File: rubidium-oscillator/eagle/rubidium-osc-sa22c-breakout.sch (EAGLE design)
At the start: 13 parts, among them J1 OSC_TMMH-109-01-G-DV-ES-A, Q1 FDN360P, Q2 FDN360P, X1 MKDSN4, X2 MPT3, X3 MPT6, X4 SMA-142-0701-801/806, X5 SMA-142-0701-801/806, X6 SMA-142-0701-801/806

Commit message: Update rubidium-osc-sa22c-breakout.sch
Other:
- note added: "NOTE: Service and Lock are active low."
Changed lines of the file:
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@@
 <text x="157.48" y="66.04" size="1.778" layer="97">LED_GREEN</text>
 <text x="157.48" y="76.2" size="1.778" layer="97">LED_RED</text>
+<text x="91.44" y="48.26" size="1.778" layer="97">NOTE: Service and Lock are active low.</text>
 </plain>
 <instances>

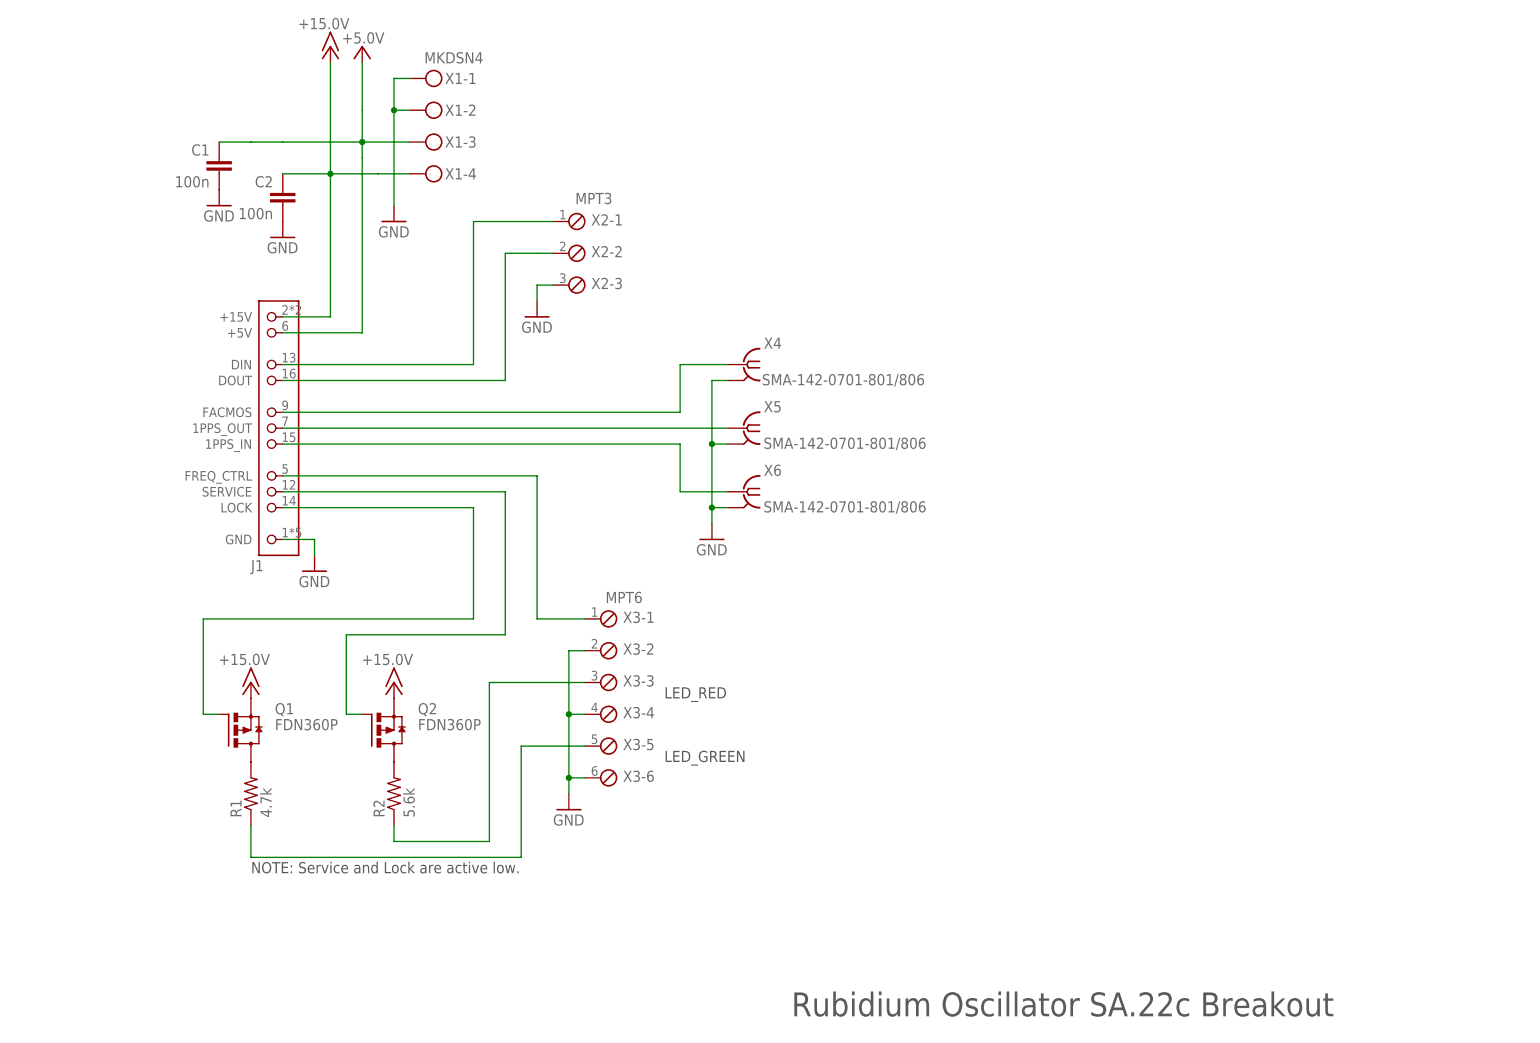
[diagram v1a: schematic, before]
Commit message: Updated rubidium osc.  Removed thermal reliefs for SMA and power grounds.  Updated p-MOSFET design.
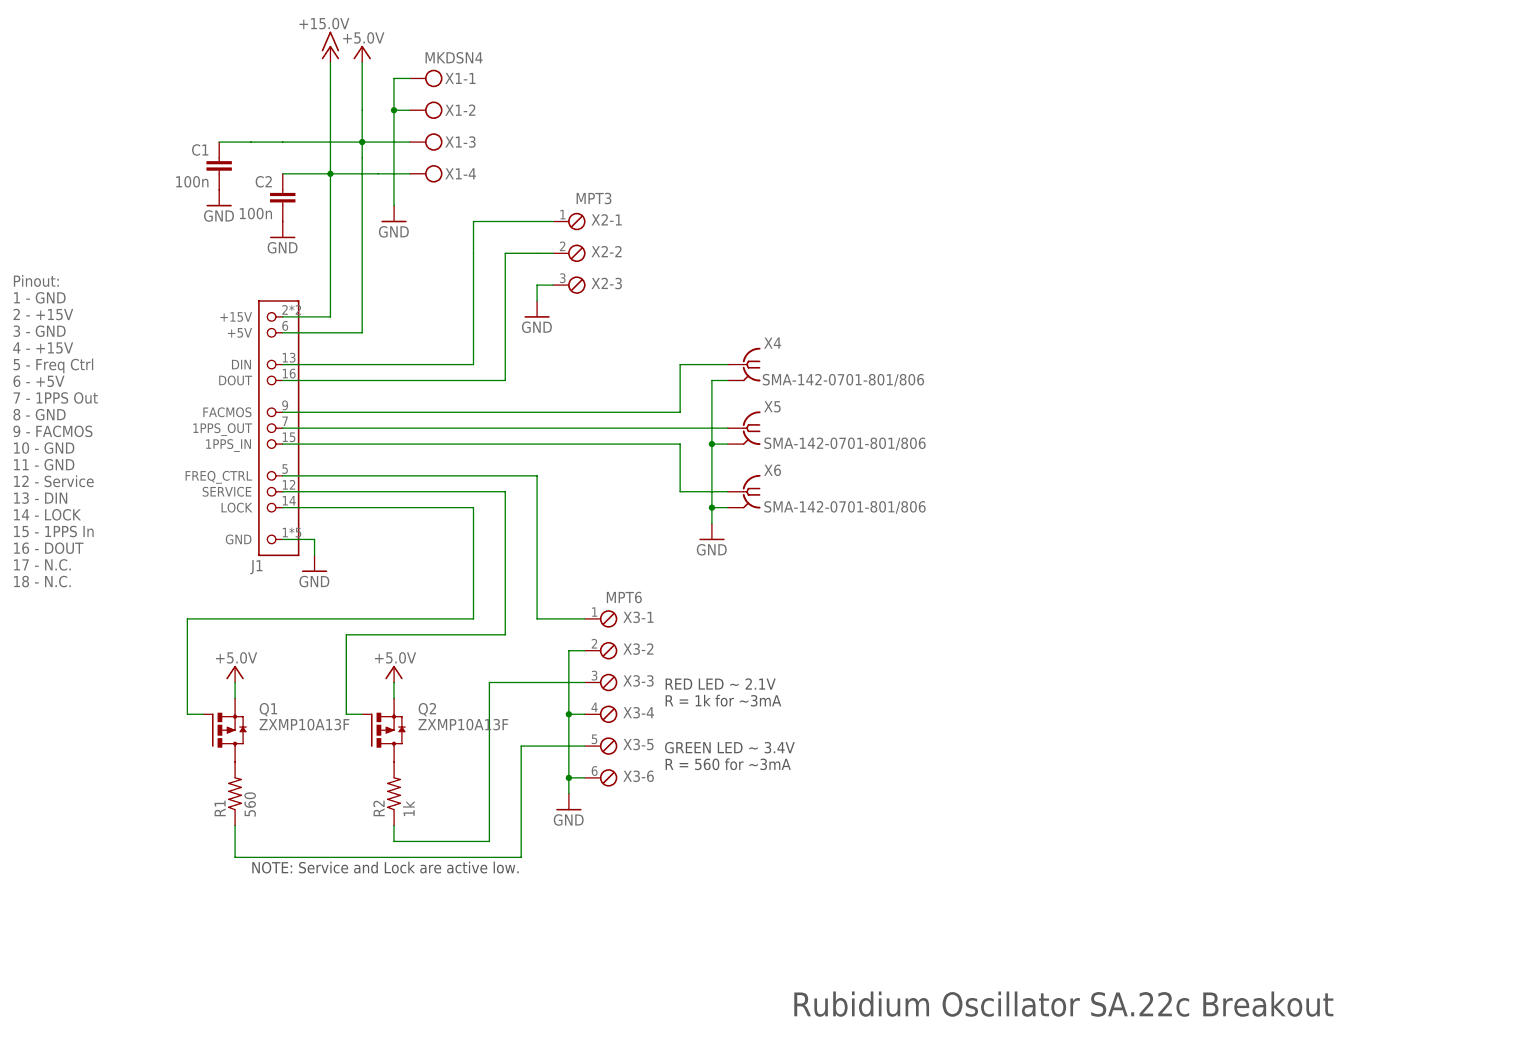
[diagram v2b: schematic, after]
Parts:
- Q1, Q2: value FDN360P -> ZXMP10A13F
- R1: value 4.7k -> 560
- R2: value 5.6k -> 1k
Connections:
- net +15V: no longer Q1.S, Q2.S
- net +5V: now also Q1.S, Q2.S
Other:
- note added: "GREEN LED ~ 3.4V R = 560 for ~3mA"
- note added: "RED LED ~ 2.1V R = 1k for ~3mA"
- note removed: "LED_GREEN"
- note removed: "LED_RED"
- moved on the sheet: Q1, R1
